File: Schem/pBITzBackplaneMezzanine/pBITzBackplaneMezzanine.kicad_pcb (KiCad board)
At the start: 4 copper layers, 99.9 x 80.4 mm, 51 parts, among them J1 USB3_A_Stacked, J2 Conn_01x04, J3 Conn_01x04, J4 10067847-001RLF, J5 Conn_02x10_Odd_Even, SW1 SW_Coded_SH-7030, SW2 SW_Coded_SH-7030, U1 FE1.1S-BSOP28BCN, U2 MAX3421EETJ_T, U3 CD74HC4050M96, U4 CD74HC4050M96, U5 74HC688, U6 74HC688, Y1 ABL-12.000MHZ-B2, Y2 ABL-12.000MHZ-B2

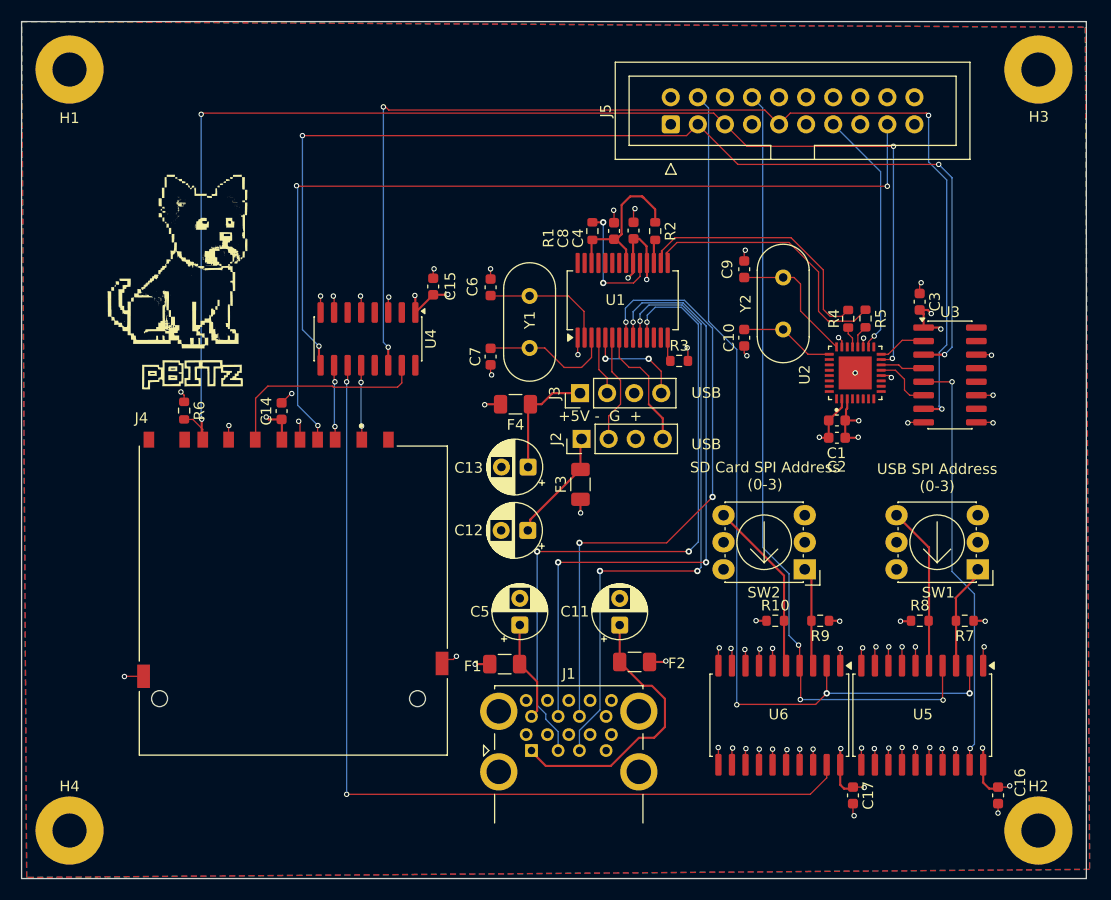
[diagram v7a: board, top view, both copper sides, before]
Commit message: Removed the rotary switch selector
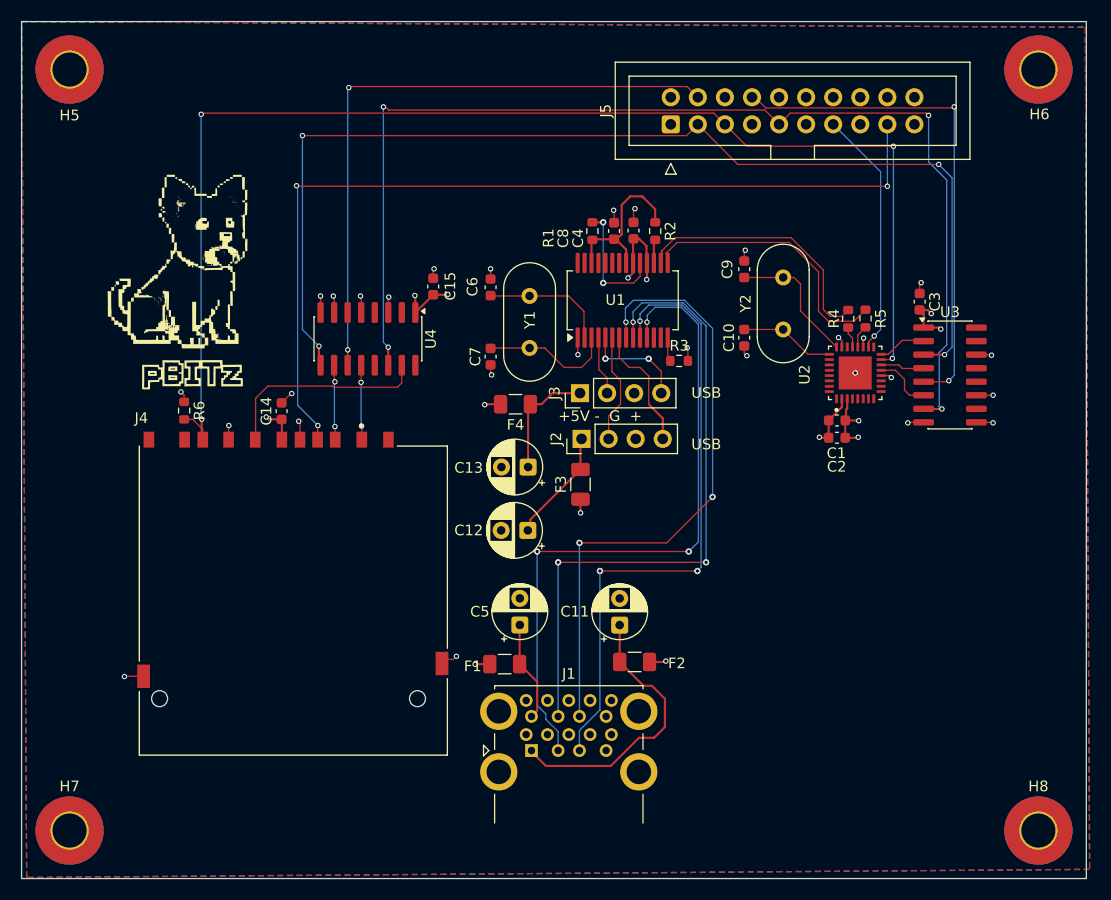
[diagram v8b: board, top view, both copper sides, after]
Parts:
- removed C16, C17: 100n, Capacitor_SMD:C_0603_1608Metric
- removed H1, H2, H3, H4: MountingHole, MountingHole:MountingHole_3.2mm_M3_Pad
- removed R10, R7, R8, R9: 4k7, Resistor_SMD:R_0603_1608Metric
- removed SW1, SW2: SW_Coded_SH-7030, Button_Switch_THT:Nidec_Copal_SH-7010C
- removed U5, U6: 74HC688, Package_SO:SOIC-20W_7.5x12.8mm_P1.27mm
- added H5: MountingHole_Pad_MP, MountingHole:MountingHole_3.2mm_M3_Pad_TopBottom, F.Cu at (379.4, 142.3)
- added H6: MountingHole_Pad_MP, MountingHole:MountingHole_3.2mm_M3_Pad_TopBottom, F.Cu at (470.3, 142.3)
- added H7: MountingHole_Pad_MP, MountingHole:MountingHole_3.2mm_M3_Pad_TopBottom, F.Cu at (379.4, 213.7)
- added H8: MountingHole_Pad_MP, MountingHole:MountingHole_3.2mm_M3_Pad_TopBottom, F.Cu at (470.3, 213.7)
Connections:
- U3 pad 5: /MezzanineConnector/~{USB_CS} -> /MezzanineConnector/SPI_CS1
- U4 pad 11: /MezzanineConnector/~{SD_CS} -> /MezzanineConnector/SPI_CS0
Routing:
- net /MezzanineConnector/~{SD_CS}: track 87.2 -> 0.00 mm, vias 2 -> 0
- net GND: track 90.9 -> 43.6 mm, vias 57 -> 27
- net /MezzanineConnector/~{USB_CS}: track 39.7 -> 0.00 mm, vias 2 -> 0
- net /MezzanineConnector/SPI_CS1: track 75.0 -> 47.7 mm, vias 3 -> 2
- net /MezzanineConnector/SPI_CS0: track 86.0 -> 59.3 mm, vias 3 -> 2
- net /MezzanineConnector/SEL3: track 16.3 -> 0.00 mm
- net +5V: track 30.4 -> 14.2 mm, vias 14 -> 6
- net /MezzanineConnector/SEL1: track 15.3 -> 0.00 mm
- net /MezzanineConnector/SEL0: track 9.30 -> 0.00 mm
- net /MezzanineConnector/SEL2: track 8.25 -> 0.00 mm
- net /USBPorts/D-: track 25.7 -> 25.0 mm
- net /USBPorts/D+: track 24.6 -> 23.9 mm
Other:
- board text removed: "SD Card SPI Address (0-3)"
- board text removed: "USB SPI Address (0-3)"
